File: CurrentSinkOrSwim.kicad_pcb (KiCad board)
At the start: 2 copper layers, 41.7 x 50.8 mm, 23 parts, among them P101 CONN_01X03, P102 CONN_01X02, P103 CONN_01X02, P201 CONN_01X01, Q201 BUK9575, U201 LMV358, U401 LM2931D-R

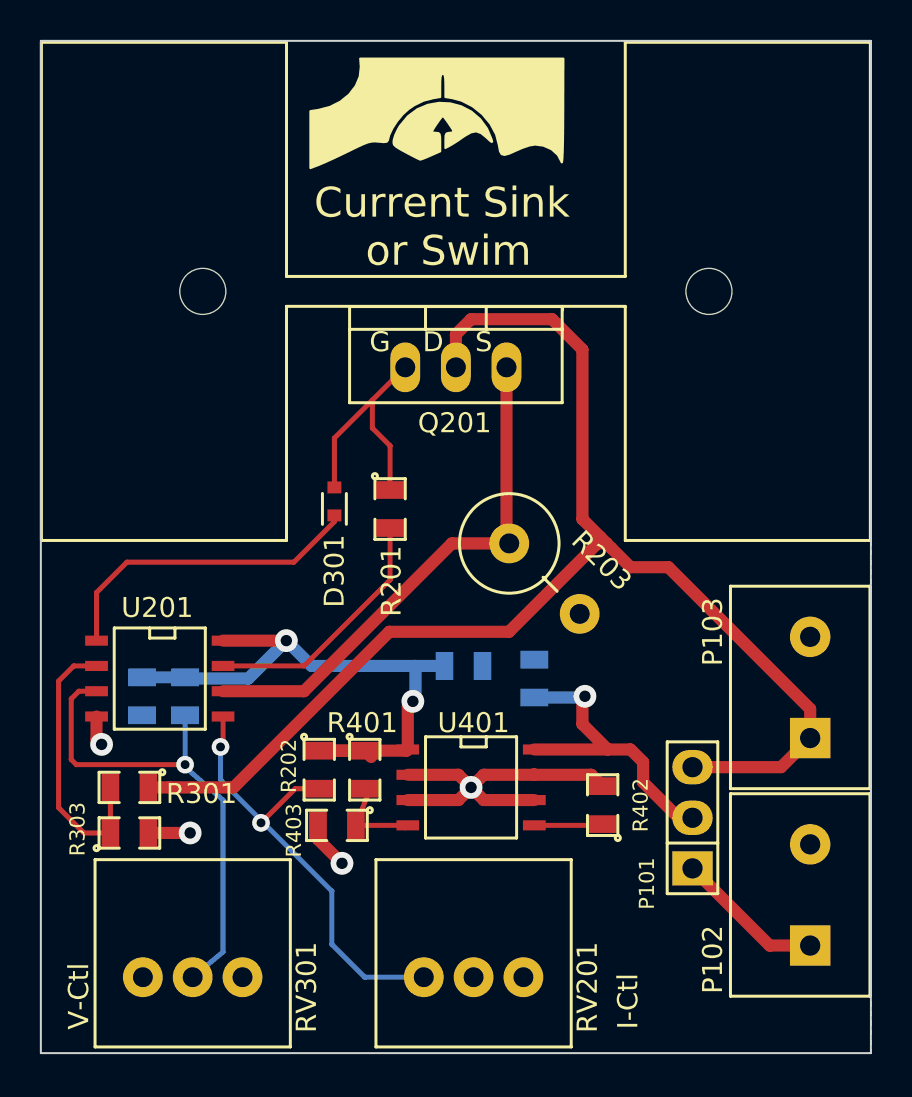
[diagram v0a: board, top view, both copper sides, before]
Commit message: Updates to the libraries for the lastest KiCad and a small update to the Datasheet
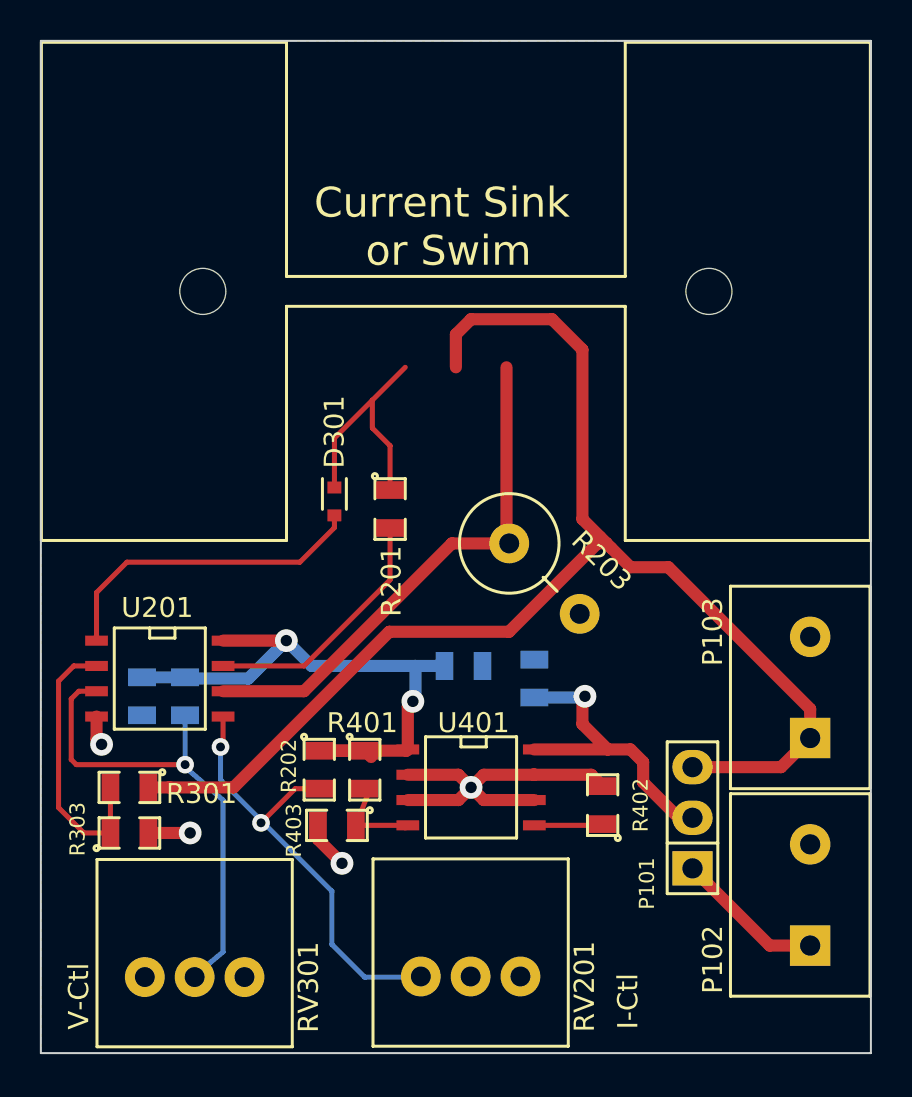
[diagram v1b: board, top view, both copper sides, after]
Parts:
- removed G***: LOGO, CSOS Local:csos-logo
- removed Q201: BUK9575, Transistors_TO-220:TO-220_FET-GDS_Vertical
- C201, C401, C402: value C -> 0.1uF
- D301: value DIODE -> 1N4148
- P201: value CONN_01X01 -> HEATSINK
- R302: value 28.7K -> 28k7
- RV201, RV301: value 10K -> 10k
- moved RV201 0.15 mm to (117.6, 89.0)
- moved RV301 0.10 mm to (103.7, 89.0)
- turned D301 to 90 degrees
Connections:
- D301 pad 1: /Current Control/FET_GATE -> Net-(D301-Pad1)
- D301 pad 2: Net-(D301-Pad2) -> /Current Control/FET_GATE
- RV201 pad 3: Net-(RV201-Pad3) -> (no net)
- RV301 pad 1: Net-(RV301-Pad1) -> (no net)
- U201 pad 1: Net-(D301-Pad2) -> Net-(D301-Pad1)
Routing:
- net Net-(D301-Pad2): track 16.3 -> 0.00 mm
- net Net-(D301-Pad1): track 0.00 -> 16.3 mm
